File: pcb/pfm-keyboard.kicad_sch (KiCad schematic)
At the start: 46 parts, among them U2 ssd1306-display

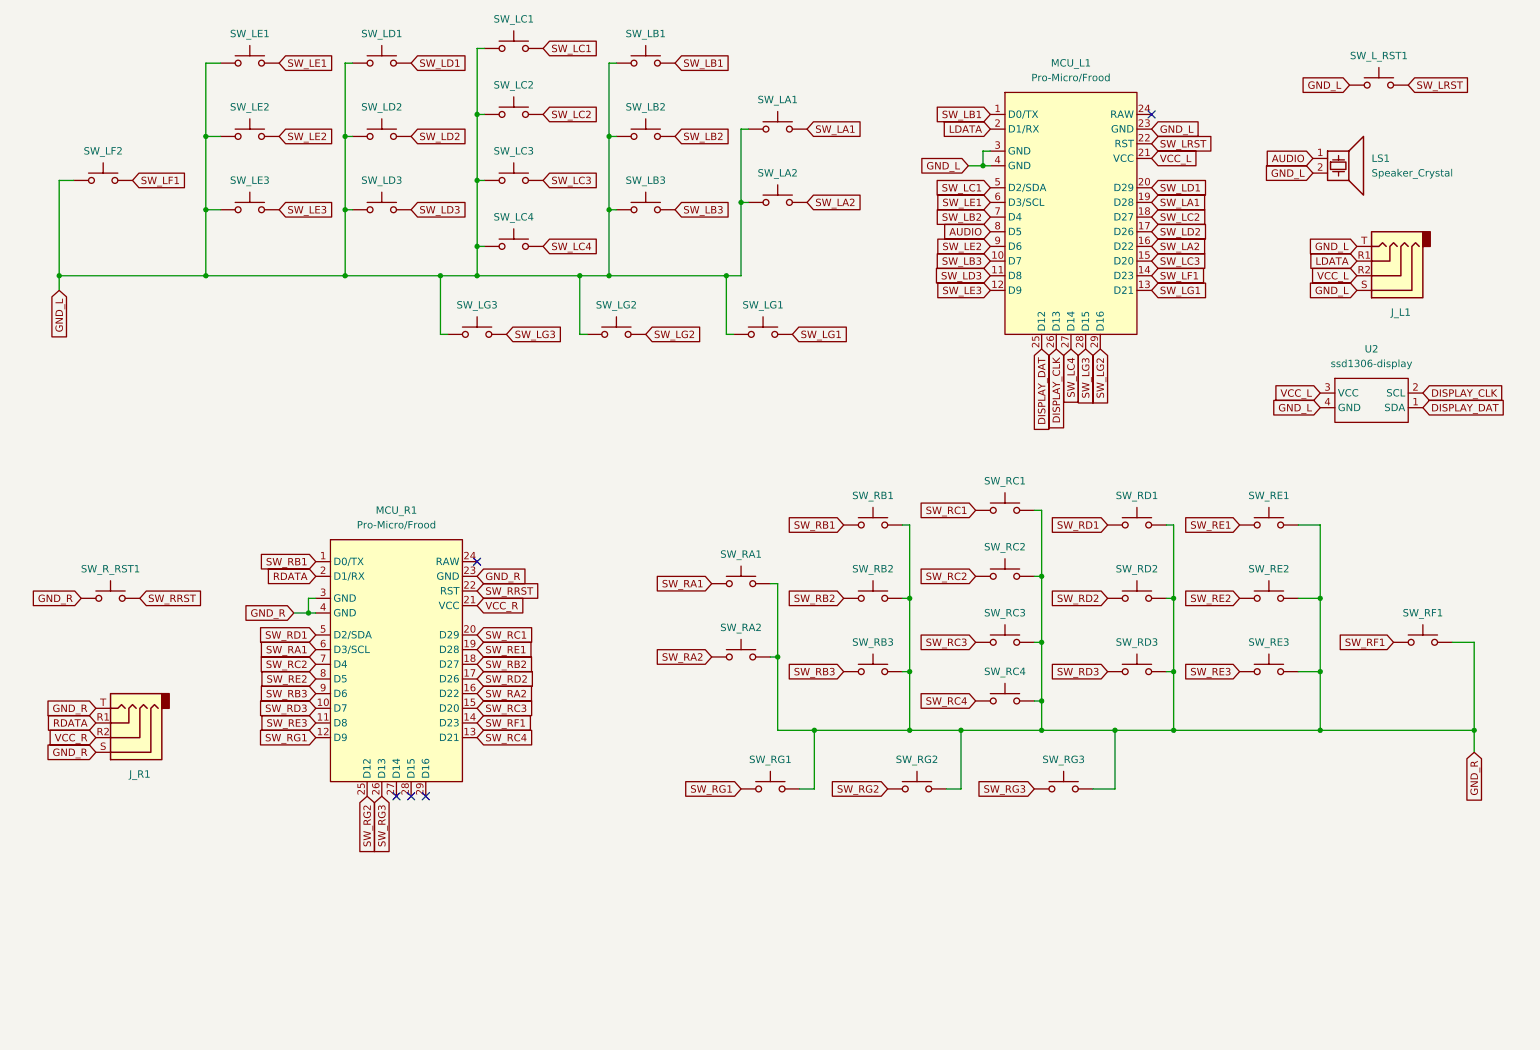
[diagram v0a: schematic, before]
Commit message: switched connections on TRRS jack for compatibility with TRS cables
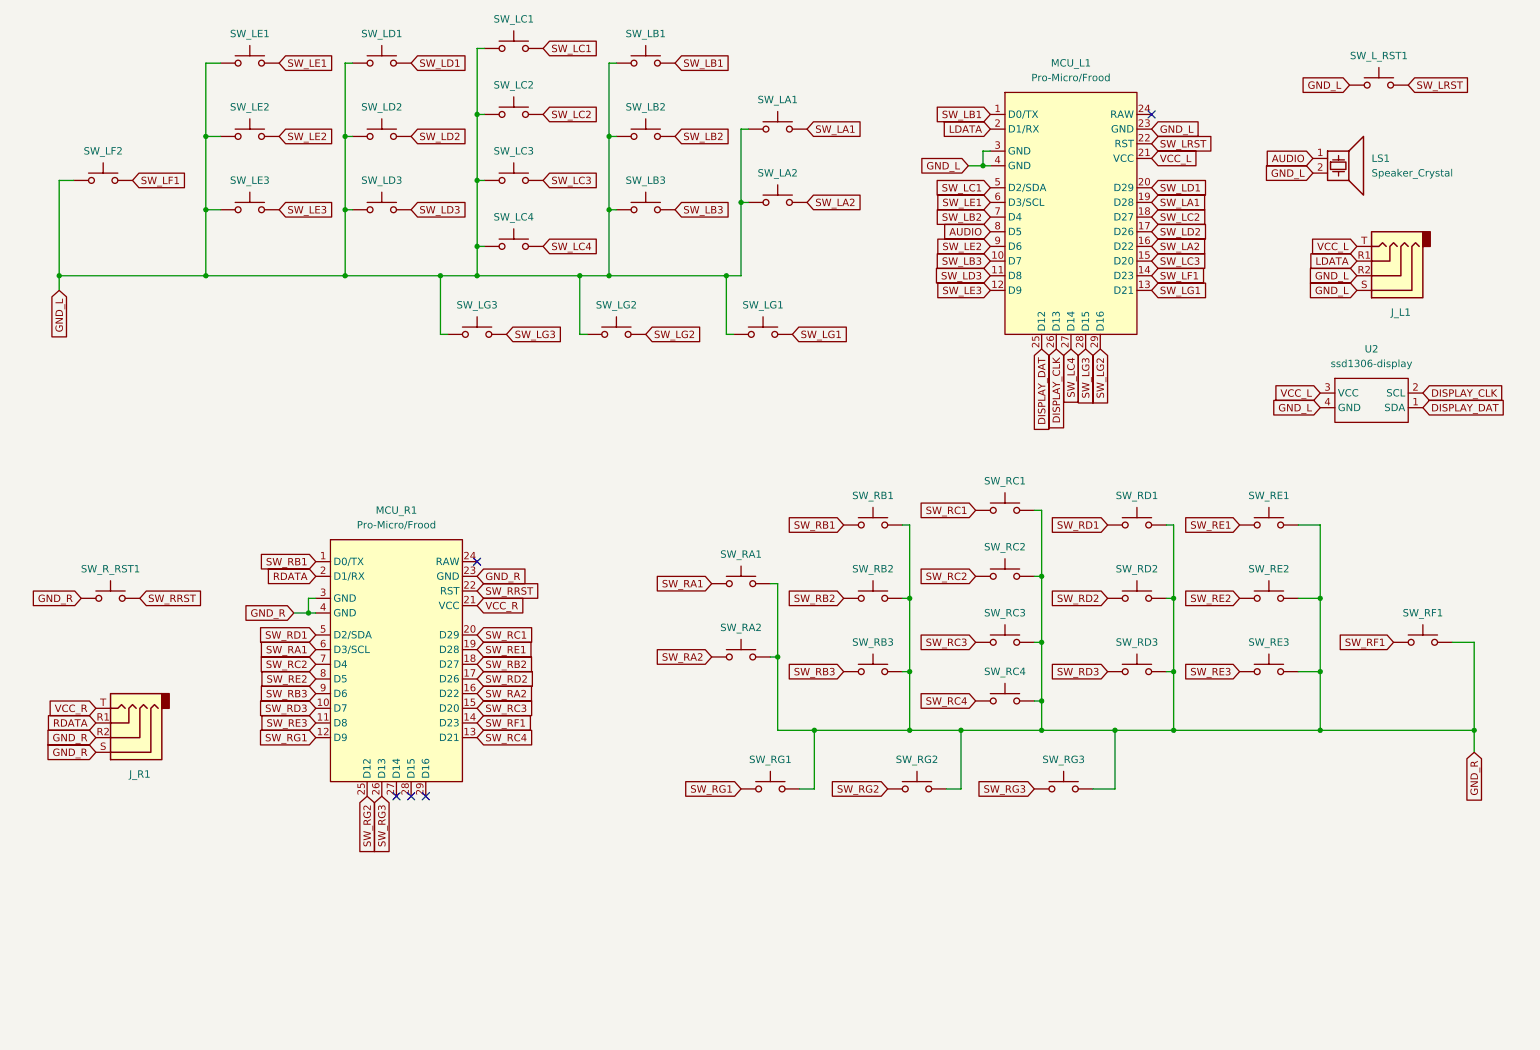
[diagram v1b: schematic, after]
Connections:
- net GND_L: now also J_L1.R2; no longer J_L1.T
- net GND_R: now also J_R1.R2; no longer J_R1.T
- net VCC_L: now also J_L1.T; no longer J_L1.R2
- net VCC_R: now also J_R1.T; no longer J_R1.R2
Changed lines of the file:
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@@
 	(global_label "GND_L"
 		(shape input)
-		(at 251.46 55.88 180)
+		(at 251.46 63.5 180)
 		(fields_autoplaced yes)
 		(effects
@@
 		)
 		(property "Intersheetrefs" "${INTERSHEET_REFS}"
-			(at 242.6086 55.88 0)
+			(at 242.6086 63.5 0)
 			(effects
 				(font
@@
 	(global_label "VCC_L"
 		(shape input)
-		(at 251.46 60.96 180)
+		(at 251.46 55.88 180)
 		(fields_autoplaced yes)
 		(effects
@@
 		)
 		(property "Intersheetrefs" "${INTERSHEET_REFS}"
-			(at 242.8505 60.96 0)
+			(at 242.8505 55.88 0)
 			(effects
 				(font
@@
 	(global_label "GND_R"
 		(shape input)
-		(at 33.02 135.89 180)
+		(at 33.02 143.51 180)
 		(fields_autoplaced yes)
 		(effects
@@
 		)
 		(property "Intersheetrefs" "${INTERSHEET_REFS}"
-			(at 23.9267 135.89 0)
+			(at 23.9267 143.51 0)
 			(effects
 				(font
@@
 	(global_label "GND_L"
 		(shape input)
-		(at 251.46 63.5 180)
+		(at 251.46 60.96 180)
 		(fields_autoplaced yes)
 		(effects
@@
 		)
 		(property "Intersheetrefs" "${INTERSHEET_REFS}"
-			(at 242.6086 63.5 0)
+			(at 242.6086 60.96 0)
 			(effects
 				(font
@@
 	(global_label "GND_R"
 		(shape input)
-		(at 33.02 143.51 180)
+		(at 33.02 140.97 180)
 		(fields_autoplaced yes)
 		(effects
@@
 		)
 		(property "Intersheetrefs" "${INTERSHEET_REFS}"
-			(at 23.9267 143.51 0)
+			(at 23.9267 140.97 0)
 			(effects
 				(font
@@
 	(global_label "VCC_R"
 		(shape input)
-		(at 33.02 140.97 180)
+		(at 33.02 135.89 180)
 		(fields_autoplaced yes)
 		(effects
@@
 		)
 		(property "Intersheetrefs" "${INTERSHEET_REFS}"
-			(at 24.1686 140.97 0)
+			(at 24.1686 135.89 0)
 			(effects
 				(font
@@
 		)
 		(instances
-			(project "diy-keyboard"
+			(project "pfm-keyboard"
 				(path "/58571878-d3b3-4b88-ba6f-b5700222d98b"
 					(reference "SW_LC4")
@@
 		)
 		(instances
-			(project "diy-keyboard"
+			(project "pfm-keyboard"
 				(path "/58571878-d3b3-4b88-ba6f-b5700222d98b"
 					(reference "SW_RG2")
@@
 		)
 		(instances
-			(project "diy-keyboard"
+			(project "pfm-keyboard"
 				(path "/58571878-d3b3-4b88-ba6f-b5700222d98b"
 					(reference "SW_RB1")
@@
 		)
 		(instances
-			(project "diy-keyboard"
+			(project "pfm-keyboard"
 				(path "/58571878-d3b3-4b88-ba6f-b5700222d98b"
 					(reference "SW_LE2")
@@
 		)
 		(instances
-			(project "diy-keyboard"
+			(project "pfm-keyboard"
 				(path "/58571878-d3b3-4b88-ba6f-b5700222d98b"
 					(reference "MCU_L1")
@@
 		)
 		(instances
-			(project "diy-keyboard"
+			(project "pfm-keyboard"
 				(path "/58571878-d3b3-4b88-ba6f-b5700222d98b"
 					(reference "SW_RB2")
@@
 		)
 		(instances
-			(project "diy-keyboard"
+			(project "pfm-keyboard"
 				(path "/58571878-d3b3-4b88-ba6f-b5700222d98b"
 					(reference "SW_RG1")
@@
 		)
 		(instances
-			(project "diy-keyboard"
+			(project "pfm-keyboard"
 				(path "/58571878-d3b3-4b88-ba6f-b5700222d98b"
 					(reference "MCU_R1")
@@
 		)
 		(instances
-			(project "diy-keyboard"
+			(project "pfm-keyboard"
 				(path "/58571878-d3b3-4b88-ba6f-b5700222d98b"
 					(reference "J_L1")
@@
 		)
 		(instances
-			(project "diy-keyboard"
+			(project "pfm-keyboard"
 				(path "/58571878-d3b3-4b88-ba6f-b5700222d98b"
 					(reference "SW_RE2")
@@
 		)
 		(instances
-			(project "diy-keyboard"
+			(project "pfm-keyboard"
 				(path "/58571878-d3b3-4b88-ba6f-b5700222d98b"
 					(reference "SW_RD3")
@@
 		)
 		(instances
-			(project "diy-keyboard"
+			(project "pfm-keyboard"
 				(path "/58571878-d3b3-4b88-ba6f-b5700222d98b"
 					(reference "SW_LB1")
@@
 		)
 		(instances
-			(project "diy-keyboard"
+			(project "pfm-keyboard"
 				(path "/58571878-d3b3-4b88-ba6f-b5700222d98b"
 					(reference "SW_LA2")
@@
 		)
 		(instances
-			(project "diy-keyboard"
+			(project "pfm-keyboard"
 				(path "/58571878-d3b3-4b88-ba6f-b5700222d98b"
 					(reference "SW_RD2")
@@
 		)
 		(instances
-			(project "diy-keyboard"
+			(project "pfm-keyboard"
 				(path "/58571878-d3b3-4b88-ba6f-b5700222d98b"
 					(reference "LS1")
@@
 		)
 		(instances
-			(project "diy-keyboard"
+			(project "pfm-keyboard"
 				(path "/58571878-d3b3-4b88-ba6f-b5700222d98b"
 					(reference "SW_LG1")
@@
 		)
 		(instances
-			(project "diy-keyboard"
+			(project "pfm-keyboard"
 				(path "/58571878-d3b3-4b88-ba6f-b5700222d98b"
 					(reference "J_R1")
@@
 		)
 		(instances
-			(project "diy-keyboard"
+			(project "pfm-keyboard"
 				(path "/58571878-d3b3-4b88-ba6f-b5700222d98b"
 					(reference "SW_LF2")
@@
 		)
 		(instances
-			(project "diy-keyboard"
+			(project "pfm-keyboard"
 				(path "/58571878-d3b3-4b88-ba6f-b5700222d98b"
 					(reference "SW_L_RST1")
@@
 		)
 		(instances
-			(project "diy-keyboard"
+			(project "pfm-keyboard"
 				(path "/58571878-d3b3-4b88-ba6f-b5700222d98b"
 					(reference "SW_LG3")
@@
 		)
 		(instances
-			(project "diy-keyboard"
+			(project "pfm-keyboard"
 				(path "/58571878-d3b3-4b88-ba6f-b5700222d98b"
 					(reference "SW_RA2")
@@
 		)
 		(instances
-			(project "diy-keyboard"
+			(project "pfm-keyboard"
 				(path "/58571878-d3b3-4b88-ba6f-b5700222d98b"
 					(reference "SW_LD2")
@@
 		)
 		(instances
-			(project "diy-keyboard"
+			(project "pfm-keyboard"
 				(path "/58571878-d3b3-4b88-ba6f-b5700222d98b"
 					(reference "SW_LC3")
@@
 		)
 		(instances
-			(project "diy-keyboard"
+			(project "pfm-keyboard"
 				(path "/58571878-d3b3-4b88-ba6f-b5700222d98b"
 					(reference "SW_LD1")
@@
 		)
 		(instances
-			(project "diy-keyboard"
+			(project "pfm-keyboard"
 				(path "/58571878-d3b3-4b88-ba6f-b5700222d98b"
 					(reference "SW_R_RST1")
@@
 		)
 		(instances
-			(project "diy-keyboard"
+			(project "pfm-keyboard"
 				(path "/58571878-d3b3-4b88-ba6f-b5700222d98b"
 					(reference "SW_LC2")
@@
 		)
 		(instances
-			(project "diy-keyboard"
+			(project "pfm-keyboard"
 				(path "/58571878-d3b3-4b88-ba6f-b5700222d98b"
 					(reference "SW_RD1")
@@
 		)
 		(instances
-			(project "diy-keyboard"
+			(project "pfm-keyboard"
 				(path "/58571878-d3b3-4b88-ba6f-b5700222d98b"
 					(reference "SW_LD3")
@@
 		)
 		(instances
-			(project "diy-keyboard"
+			(project "pfm-keyboard"
 				(path "/58571878-d3b3-4b88-ba6f-b5700222d98b"
 					(reference "SW_LB3")
@@
 		)
 		(instances
-			(project "diy-keyboard"
+			(project "pfm-keyboard"
 				(path "/58571878-d3b3-4b88-ba6f-b5700222d98b"
 					(reference "SW_LA1")
@@
 		)
 		(instances
-			(project "diy-keyboard"
+			(project "pfm-keyboard"
 				(path "/58571878-d3b3-4b88-ba6f-b5700222d98b"
 					(reference "SW_RC1")
@@
 		)
 		(instances
-			(project "diy-keyboard"
+			(project "pfm-keyboard"
 				(path "/58571878-d3b3-4b88-ba6f-b5700222d98b"
 					(reference "SW_RF1")
@@
 		)
 		(instances
-			(project "diy-keyboard"
+			(project "pfm-keyboard"
 				(path "/58571878-d3b3-4b88-ba6f-b5700222d98b"
 					(reference "SW_RE1")
@@
 		)
 		(instances
-			(project "diy-keyboard"
+			(project "pfm-keyboard"
 				(path "/58571878-d3b3-4b88-ba6f-b5700222d98b"
 					(reference "SW_LC1")
@@
 		)
 		(instances
-			(project "diy-keyboard"
+			(project "pfm-keyboard"
 				(path "/58571878-d3b3-4b88-ba6f-b5700222d98b"
 					(reference "SW_LG2")
@@
 		)
 		(instances
-			(project "diy-keyboard"
+			(project "pfm-keyboard"
 				(path "/58571878-d3b3-4b88-ba6f-b5700222d98b"
 					(reference "SW_RC3")
@@
 		)
 		(instances
-			(project "diy-keyboard"
+			(project "pfm-keyboard"
 				(path "/58571878-d3b3-4b88-ba6f-b5700222d98b"
 					(reference "SW_LE3")
@@
 		)
 		(instances
-			(project "diy-keyboard"
+			(project "pfm-keyboard"
 				(path "/58571878-d3b3-4b88-ba6f-b5700222d98b"
 					(reference "SW_RC4")
@@
 		)
 		(instances
-			(project "diy-keyboard"
+			(project "pfm-keyboard"
 				(path "/58571878-d3b3-4b88-ba6f-b5700222d98b"
 					(reference "SW_RA1")
@@
 		)
 		(instances
-			(project "diy-keyboard"
+			(project "pfm-keyboard"
 				(path "/58571878-d3b3-4b88-ba6f-b5700222d98b"
 					(reference "SW_RE3")
@@
 		)
 		(instances
-			(project "diy-keyboard"
+			(project "pfm-keyboard"
 				(path "/58571878-d3b3-4b88-ba6f-b5700222d98b"
 					(reference "SW_RC2")
@@
 		)
 		(instances
-			(project "diy-keyboard"
+			(project "pfm-keyboard"
 				(path "/58571878-d3b3-4b88-ba6f-b5700222d98b"
 					(reference "U2")
@@
 		)
 		(instances
-			(project "diy-keyboard"
+			(project "pfm-keyboard"
 				(path "/58571878-d3b3-4b88-ba6f-b5700222d98b"
 					(reference "SW_LE1")
@@
 		)
 		(instances
-			(project "diy-keyboard"
+			(project "pfm-keyboard"
 				(path "/58571878-d3b3-4b88-ba6f-b5700222d98b"
 					(reference "SW_RG3")
@@
 		)
 		(instances
-			(project "diy-keyboard"
+			(project "pfm-keyboard"
 				(path "/58571878-d3b3-4b88-ba6f-b5700222d98b"
 					(reference "SW_RB3")
@@
 		)
 		(instances
-			(project "diy-keyboard"
+			(project "pfm-keyboard"
 				(path "/58571878-d3b3-4b88-ba6f-b5700222d98b"
 					(reference "SW_LB2")

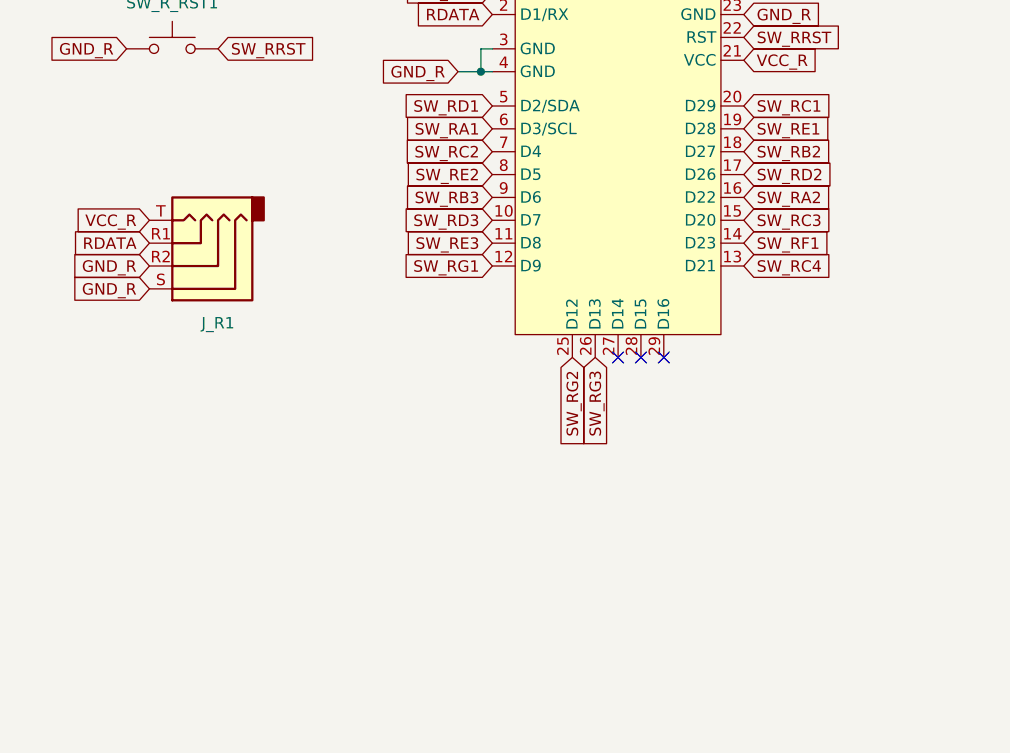
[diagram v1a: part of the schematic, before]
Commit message: Use same MCU pins on left and right to avoid problems when right is master. Added mounting holes to schematic.
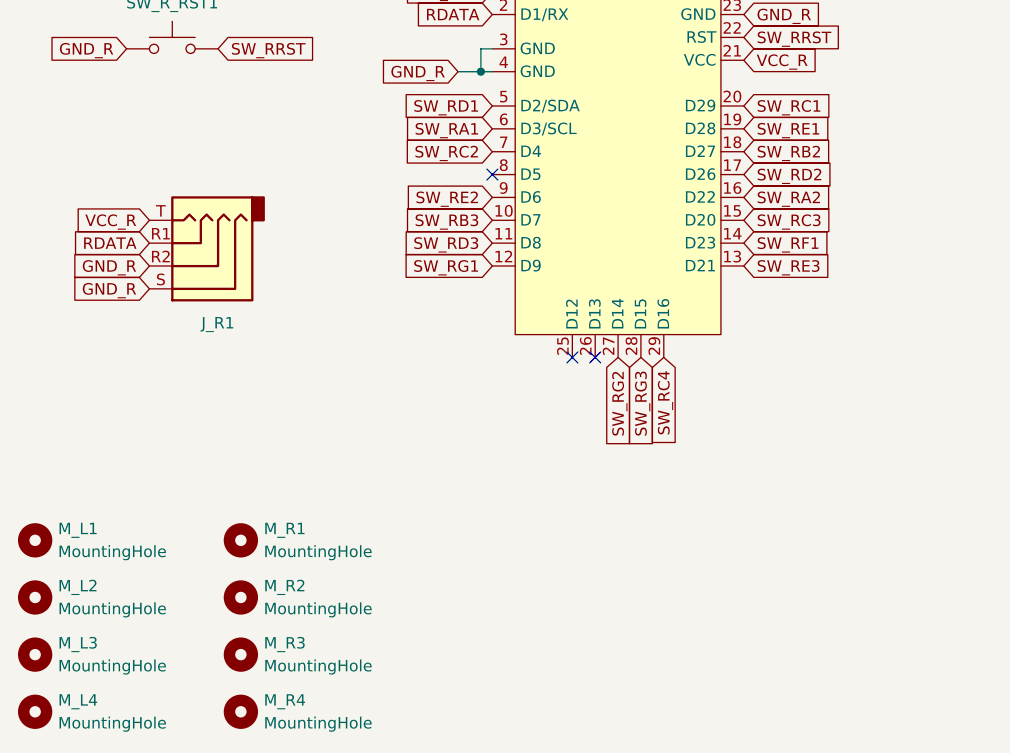
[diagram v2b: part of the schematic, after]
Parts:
- added M_L1, M_L2, M_L3, M_L4, M_R1, M_R2, M_R3, M_R4: MountingHole, MountingHole:MountingHole_2.7mm_M2.5, symbol Mechanical:MountingHole
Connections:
- net SW_RB3: now also MCU_R1.10 (D7); no longer MCU_R1.9 (D6)
- net SW_RC4: now also MCU_R1.29 (D16); no longer MCU_R1.13 (D21)
- net SW_RD3: now also MCU_R1.11 (D8); no longer MCU_R1.10 (D7)
- net SW_RE2: now also MCU_R1.9 (D6); no longer MCU_R1.8 (D5)
- net SW_RE3: now also MCU_R1.13 (D21); no longer MCU_R1.11 (D8)
- net SW_RG2: now also MCU_R1.27 (D14); no longer MCU_R1.25 (D12)
- net SW_RG3: now also MCU_R1.28 (D15); no longer MCU_R1.26 (D13)
